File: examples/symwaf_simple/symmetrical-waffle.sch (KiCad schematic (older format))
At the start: 9 parts, among them J3 GPIO Header, SW2 SW_DIP_x01, U1 ATMEGA328-AU, Y1 Crystal

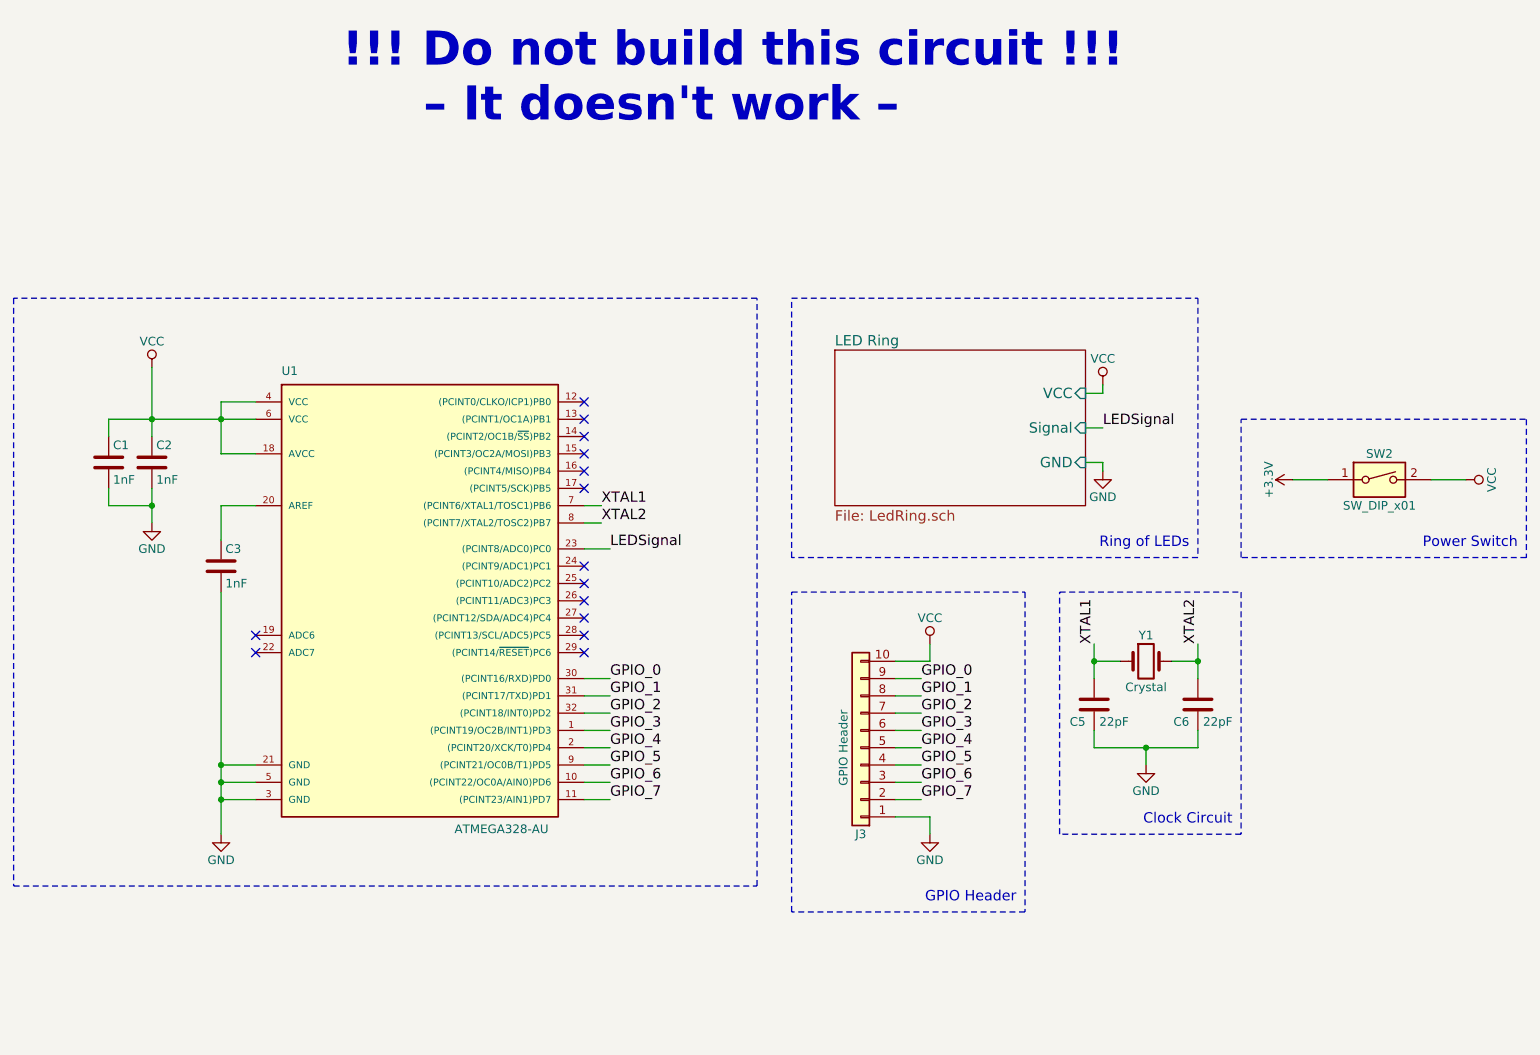
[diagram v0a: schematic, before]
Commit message: Creating a simpler version of the example board
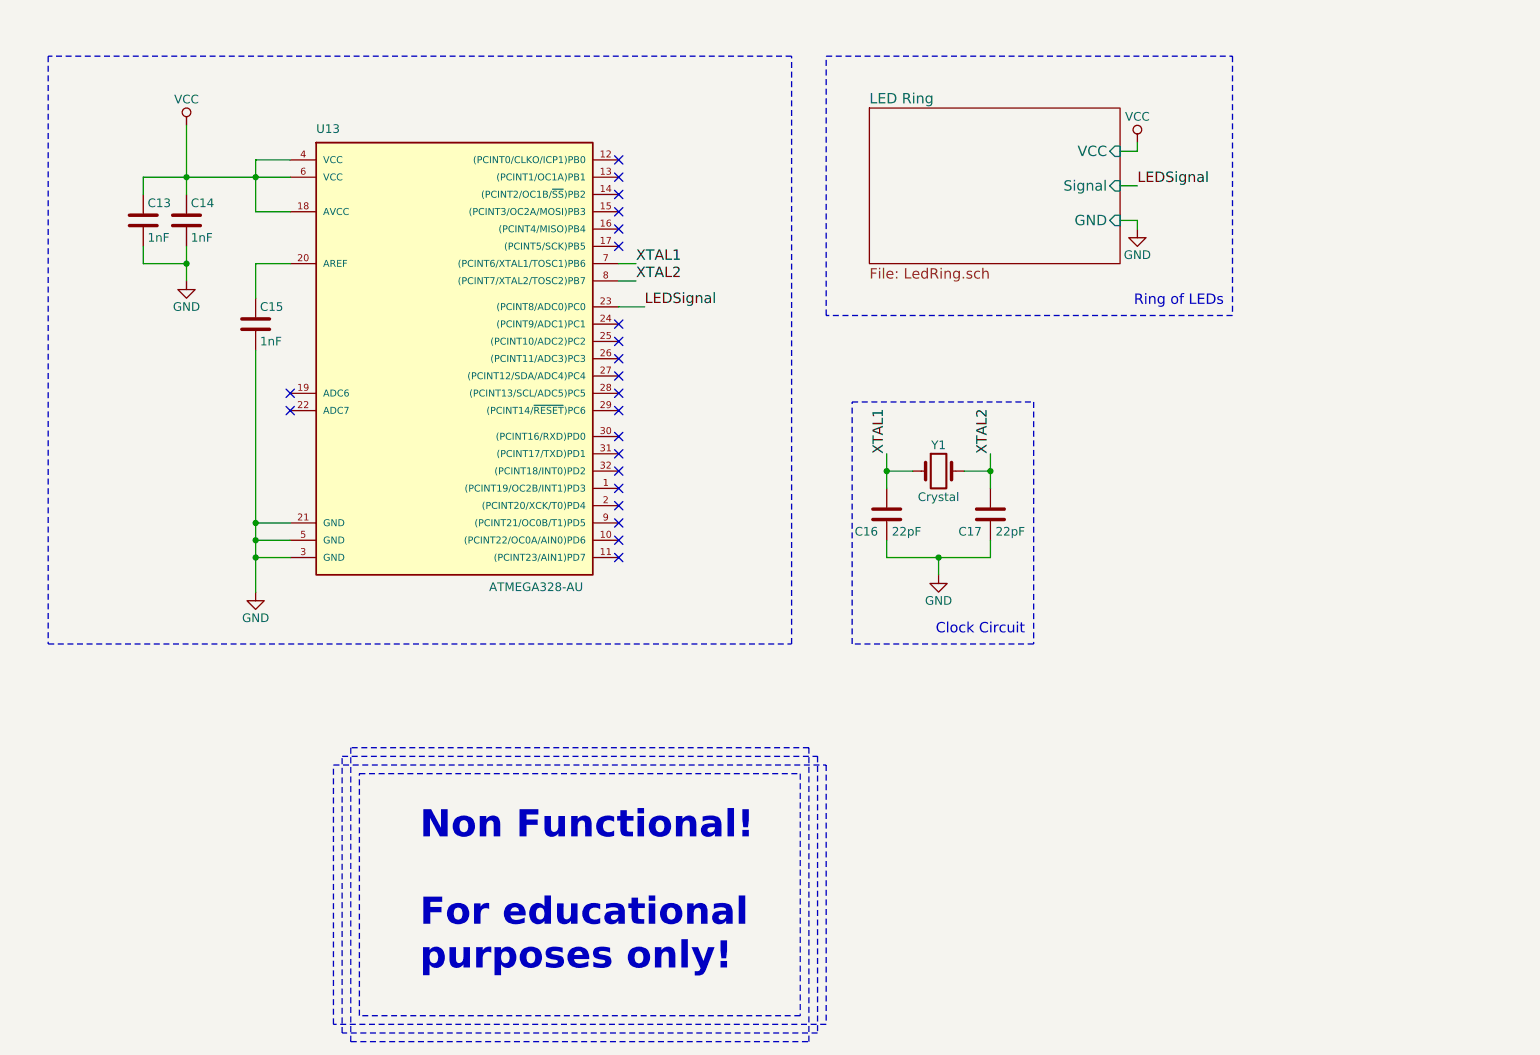
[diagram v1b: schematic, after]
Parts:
- removed J3: GPIO Header, Pin_Headers:Pin_Header_Straight_1x10_Pitch1.00mm, symbol Conn_01x10
- removed SW2: SW_DIP_x01, Buttons_Switches_THT:SW_DIP_x1_W7.62mm_Piano, symbol SW_DIP_x01
- C13: renamed from C1; footprint Capacitors_SMD:C_0805 -> Capacitors_SMD:C_1206
- C14: renamed from C2; footprint Capacitors_SMD:C_0805 -> Capacitors_SMD:C_1206
- C15: renamed from C3; footprint Capacitors_SMD:C_0805 -> Capacitors_SMD:C_1206
- C16: renamed from C5; footprint Capacitors_SMD:C_0805 -> Capacitors_SMD:C_1206
- C17: renamed from C6; footprint Capacitors_SMD:C_0805 -> Capacitors_SMD:C_1206
- Y1: footprint Crystals:Crystal_AT310_d3.0mm_l10.0mm_Horizontal -> Crystals:Crystal_SMD_2012-2pin_2.0x1.2mm_HandSoldering
- renumbered U1 to U13
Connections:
- net GPIO_0: no longer names the net of U13.30 ((PCINT16/RXD)PD0)
- net GPIO_1: no longer names the net of U13.31 ((PCINT17/TXD)PD1)
- net GPIO_2: no longer names the net of U13.32 ((PCINT18/INT0)PD2)
- net GPIO_3: no longer names the net of U13.1 ((PCINT19/OC2B/INT1)PD3)
- net GPIO_4: no longer names the net of U13.2 ((PCINT20/XCK/T0)PD4)
- net GPIO_5: no longer names the net of U13.9 ((PCINT21/OC0B/T1)PD5)
- net GPIO_6: no longer names the net of U13.10 ((PCINT22/OC0A/AIN0)PD6)
- net GPIO_7: no longer names the net of U13.11 ((PCINT23/AIN1)PD7)
- no-connect marks 14 -> 22
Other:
- note added: "Non Functional!\n\nFor educational \npurposes only!"
- note removed: "!!! Do not build this circuit !!!\n – It doesn't work –"
- note removed: "GPIO Header"
- note removed: "Power Switch"
- moved on the sheet: C13, C14, C15, C16, C17, U13, Y1
